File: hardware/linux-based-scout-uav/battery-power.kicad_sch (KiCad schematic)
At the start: 1 part, among them J1 XT60PW-M

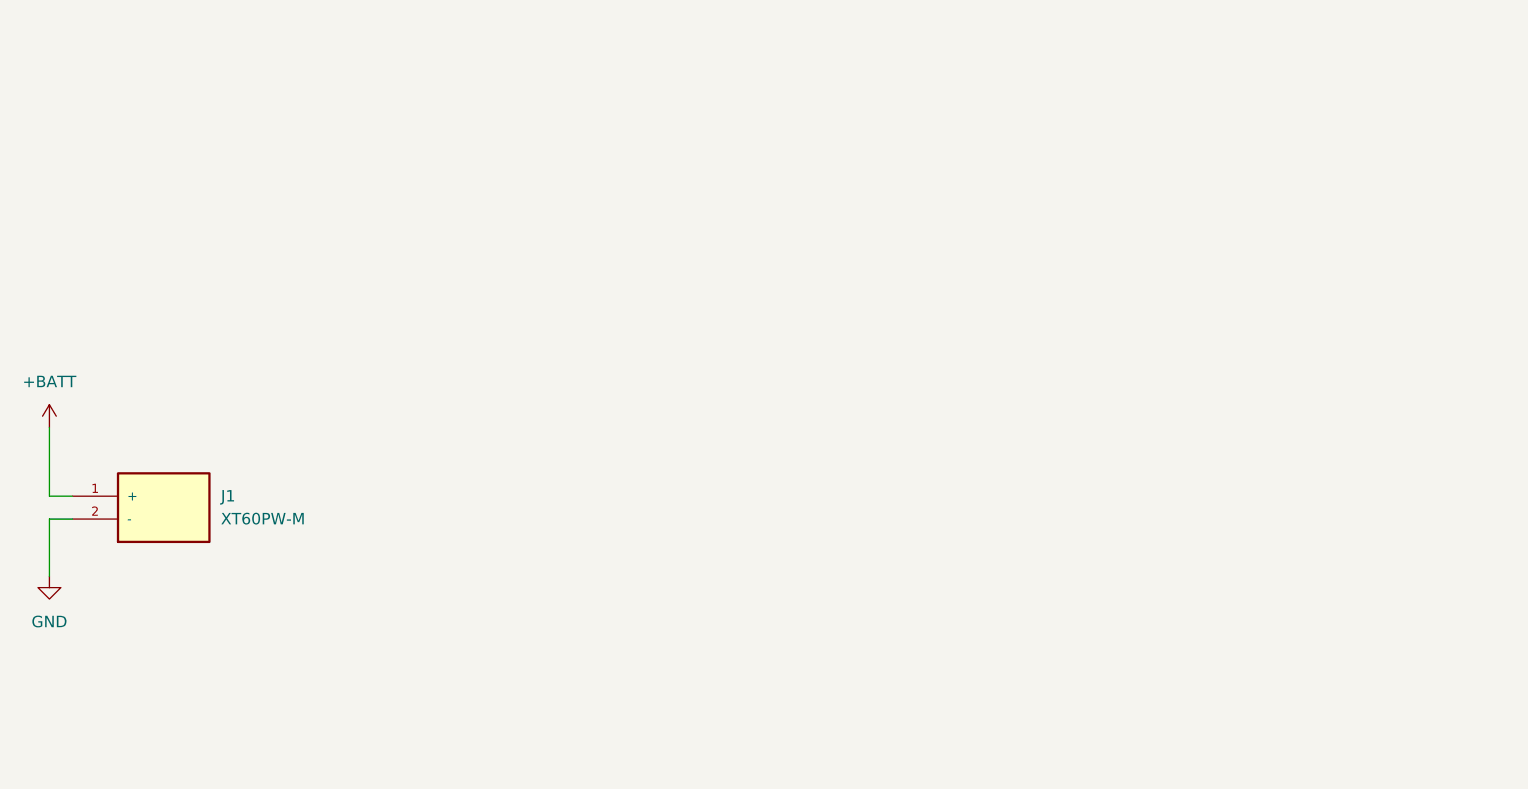
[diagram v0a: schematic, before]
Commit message: Updates (Schematic, Readme, doc)
Updates to Schematic capture, README file and doc files.
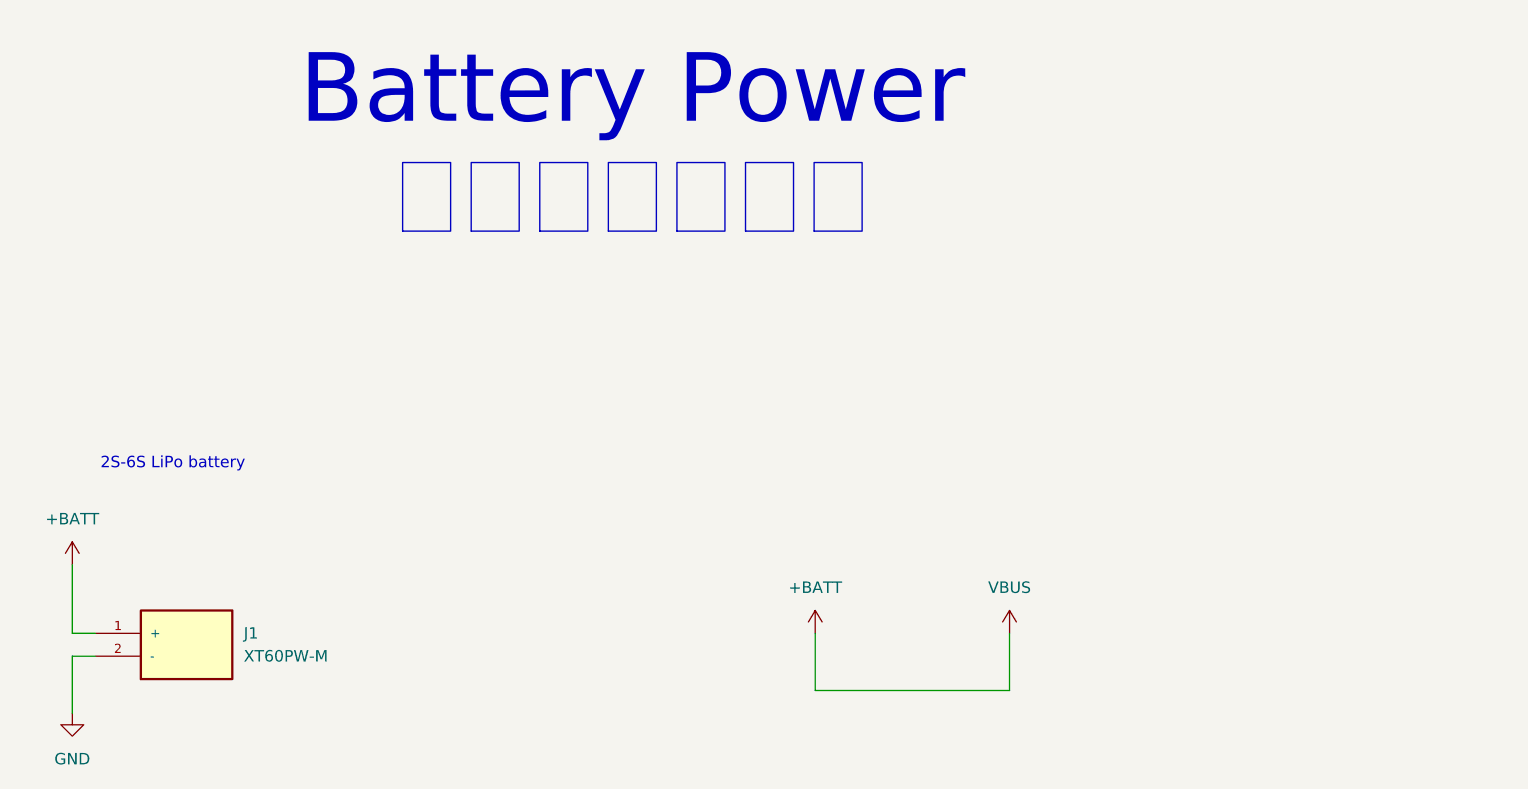
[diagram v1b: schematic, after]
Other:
- note added: "2S-6S LiPo battery"
- note added: "Battery Power バッテリー電源"
- moved on the sheet: J1

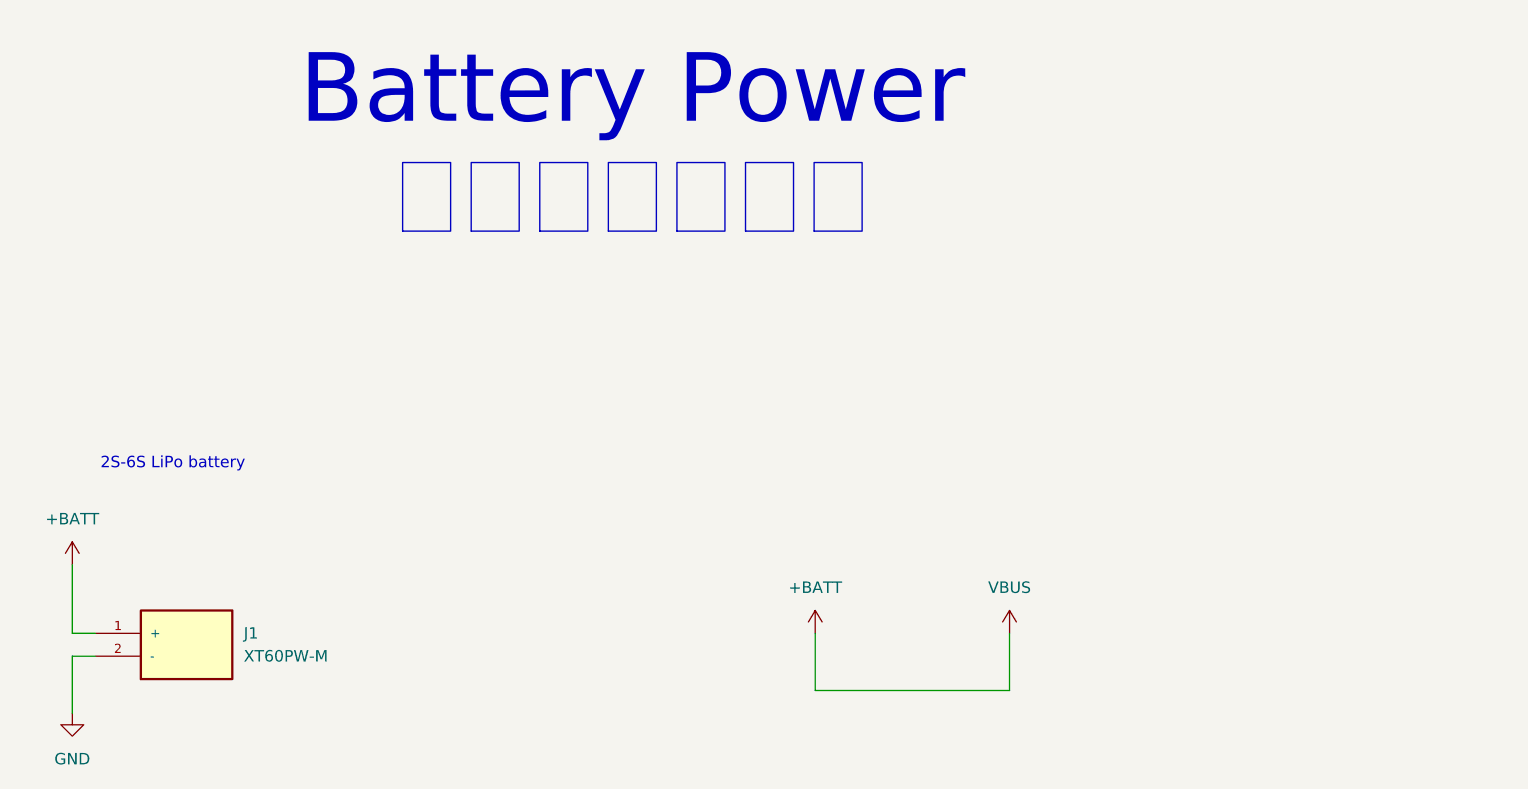
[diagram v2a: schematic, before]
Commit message: Schematic updates
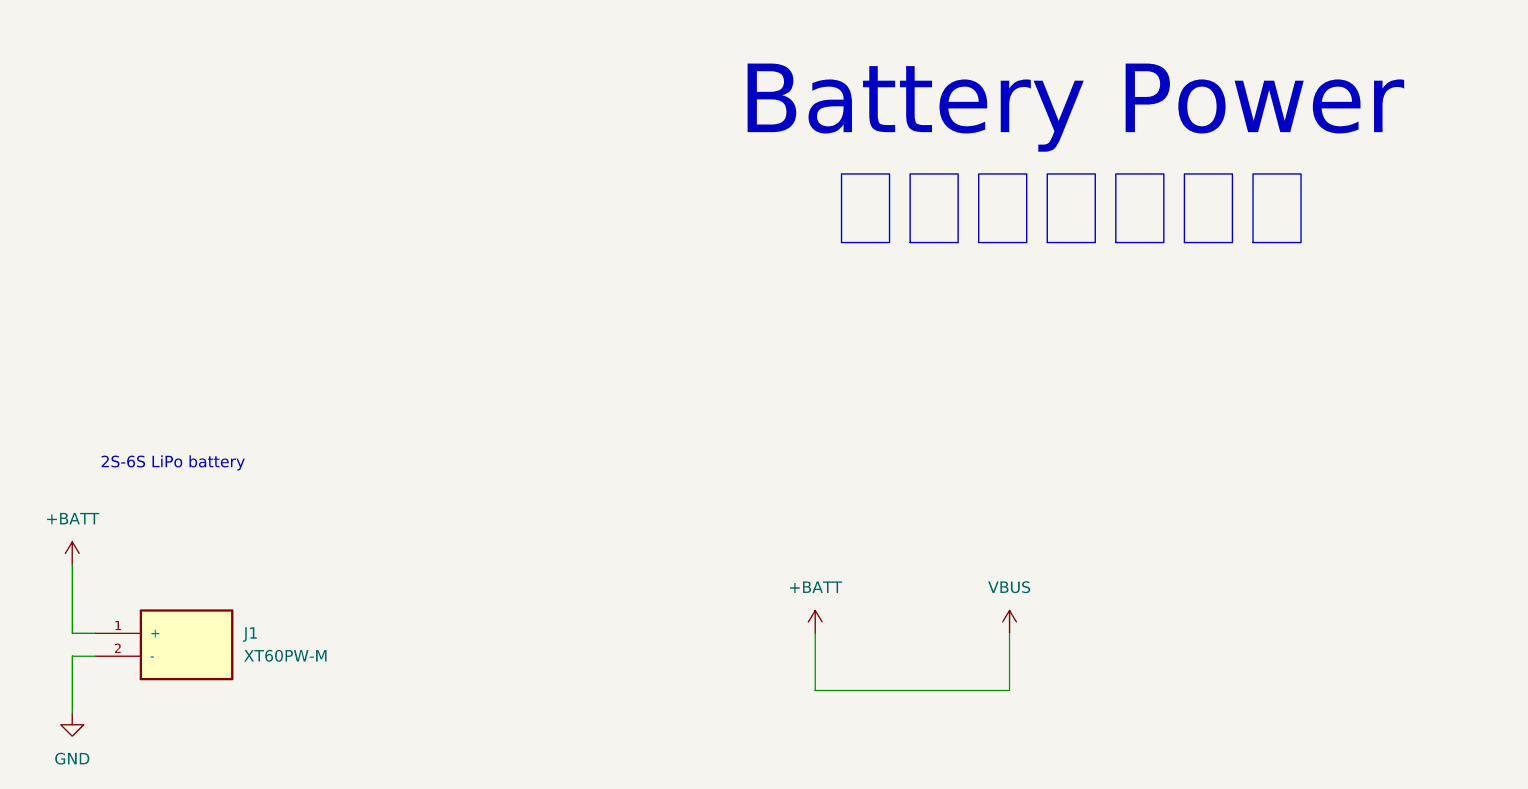
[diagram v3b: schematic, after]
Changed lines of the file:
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@@
 	(text "Battery Power\nバッテリー電源"
 		(exclude_from_sim no)
-		(at 152.4 25.908 0)
+		(at 201.168 27.178 0)
 		(effects
 			(font
